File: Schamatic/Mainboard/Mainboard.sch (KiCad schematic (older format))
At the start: 70 parts, among them J1 CONN_01X02, J2 CONN_01X02, J3 CONN_01X02, J4 CONN_01X02, J5 CONN_01X02, J6 CONN_02X05, J7 CONN_02X20, Q1 Q_NMOS_GDS, Q2 PSMN014-40YS, U1 IFX91041 - 3.3V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

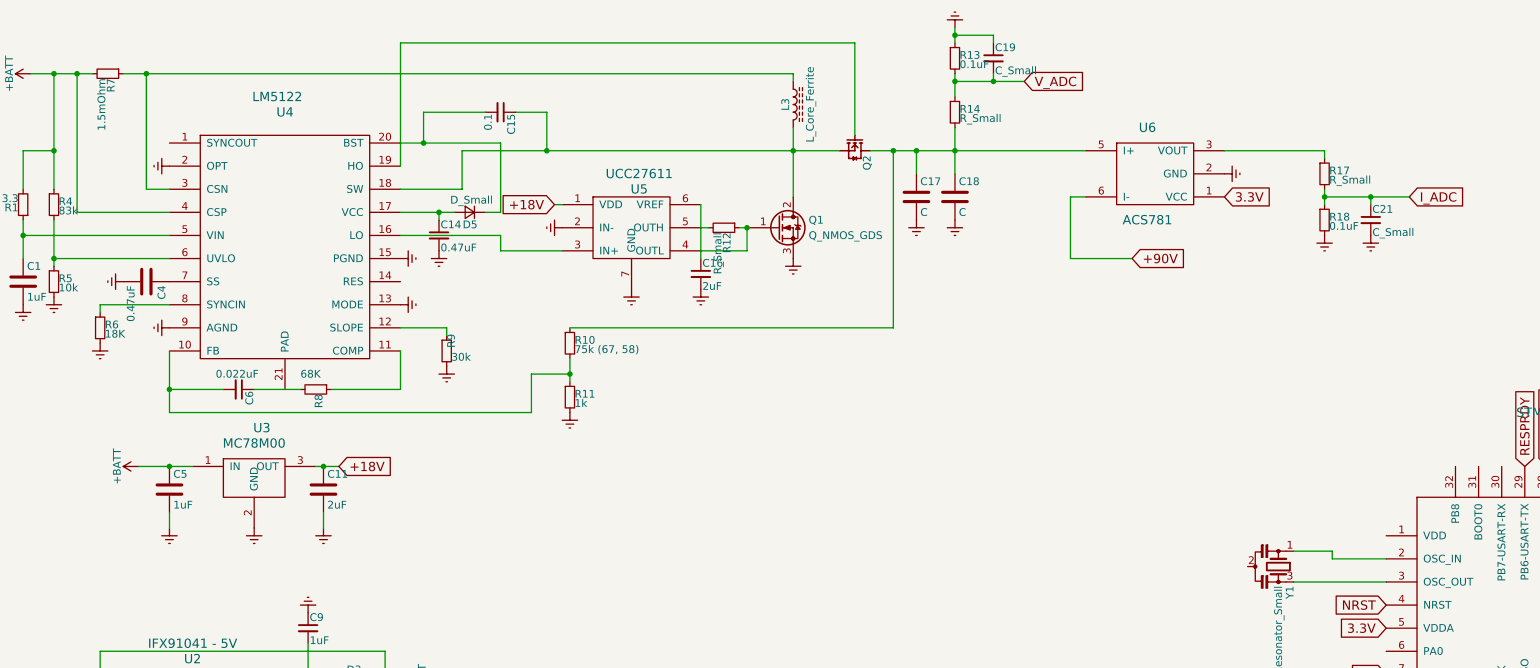
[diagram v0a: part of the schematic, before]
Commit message: components allocated
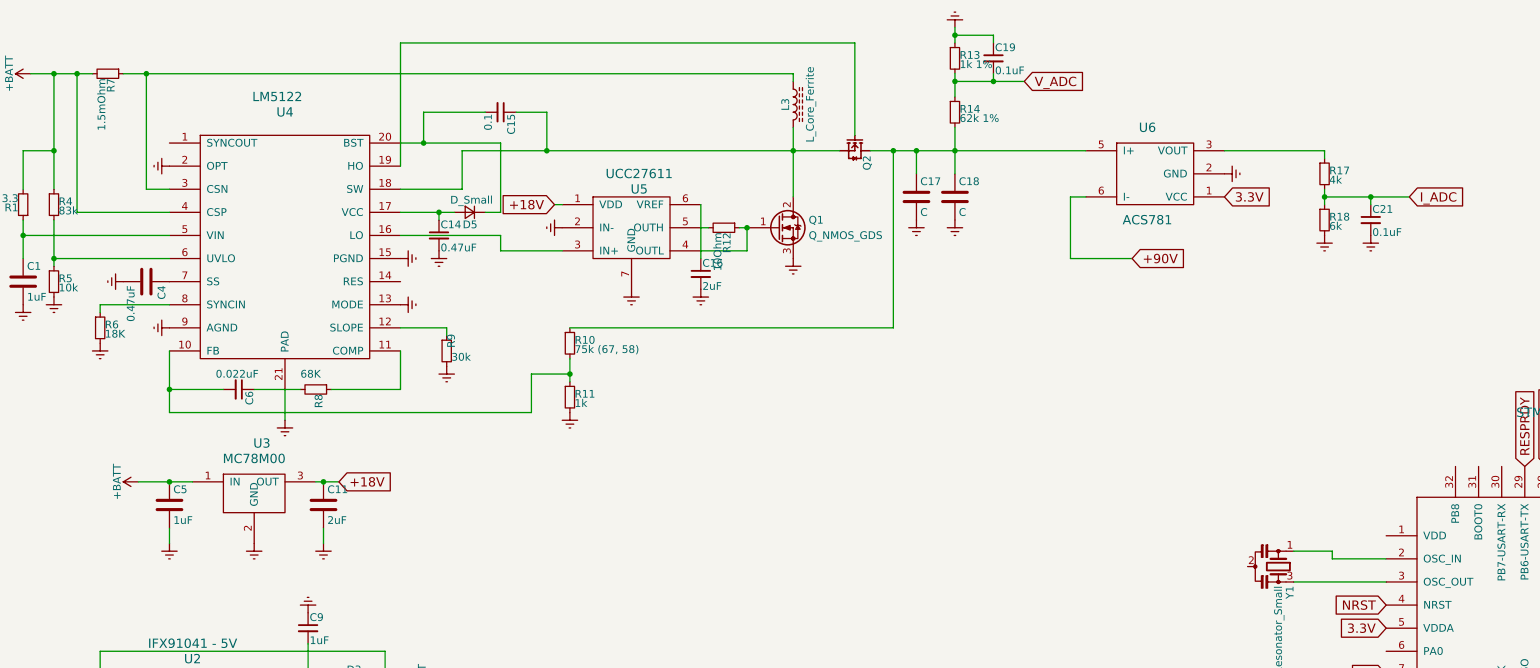
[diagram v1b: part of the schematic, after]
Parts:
- C19, C21: value C_Small -> 0.1uF
- J3: footprint (none) -> Dizzy:XT60
- J4, J5: footprint (none) -> Dizzy:xt30
- L3: footprint (none) -> Dizzy:PQ3218‐3R3‐70‐T
- Q1: footprint (none) -> Dizzy:EPC2022
- R12: value R_Small -> 10Ohm; footprint (none) -> Resistors_SMD:R_0603
- R13: value 0.1uF -> 1k 1%; footprint (none) -> Resistors_SMD:R_0603
- R14: value R_Small -> 62k 1%; footprint (none) -> Resistors_SMD:R_0603
- R15, R16, R19, R20: footprint (none) -> Resistors_SMD:R_0603
- R17: value R_Small -> 4k; footprint (none) -> Resistors_SMD:R_0603
- R18: value 0.1uF -> 6k; footprint (none) -> Resistors_SMD:R_0603
- U1, U2: footprint (none) -> Housings_SOIC:HTSOP-8-1EP_3.9x4.9mm_Pitch1.27mm_ThermalVias
- U3: footprint (none) -> TO_SOT_Packages_SMD:TO-252-2
- U4: footprint (none) -> Housings_SSOP:HTSSOP-20-1EP_4.4x6.5mm_Pitch0.65mm_ThermalPad
- U5: footprint (none) -> Housings_DFN_QFN:DFN-6-1EP_2x2mm_Pitch0.65mm
- U6: footprint (none) -> Dizzy:ACS781
- U7: footprint (none) -> Dizzy:LGA16R50P3X5_300X300X100
- U8: footprint (none) -> Dizzy:UFQFPN32-small-pad
- U9: footprint (none) -> Dizzy:LTC2876
- Y1: footprint (none) -> Dizzy:Oscillator
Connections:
- net Earth: now also U4.21 (PAD)
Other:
- moved on the sheet: C11, C5, U3

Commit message: started mainboard PCB
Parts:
- added C22: 2uF, Capacitors_SMD:C_1812, symbol C_Small
- added J8, J9: CONN_01X02, Pin_Headers:Pin_Header_Straight_1x02_Pitch2.54mm, symbol CONN_01X02
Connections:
- net +BATT: now also C22.1
- net 3.3V: now also J8.2 (P2)
- net 5V: now also J9.2 (P2)
- net Earth: now also C22.2, J8.1 (P1), J9.1 (P1)
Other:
- moved on the sheet: C1, C14, C15, C16, C17, C18, C19, C21, C4, C6, D5, L3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
